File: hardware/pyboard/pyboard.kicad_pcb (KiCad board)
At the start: 2 copper layers, 65 parts, among them J1 Battery, J2 Arduino_Mega2560_Shield, J6 USB_B_Micro, J9 Micro_SD_SCHA5B0200, Q1 IRLML6402, Q2 IRLML6402, SW1 RST, SW2 USR, U1 STM32F405RGT6, U2 MCP1703A-3302_SOT89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

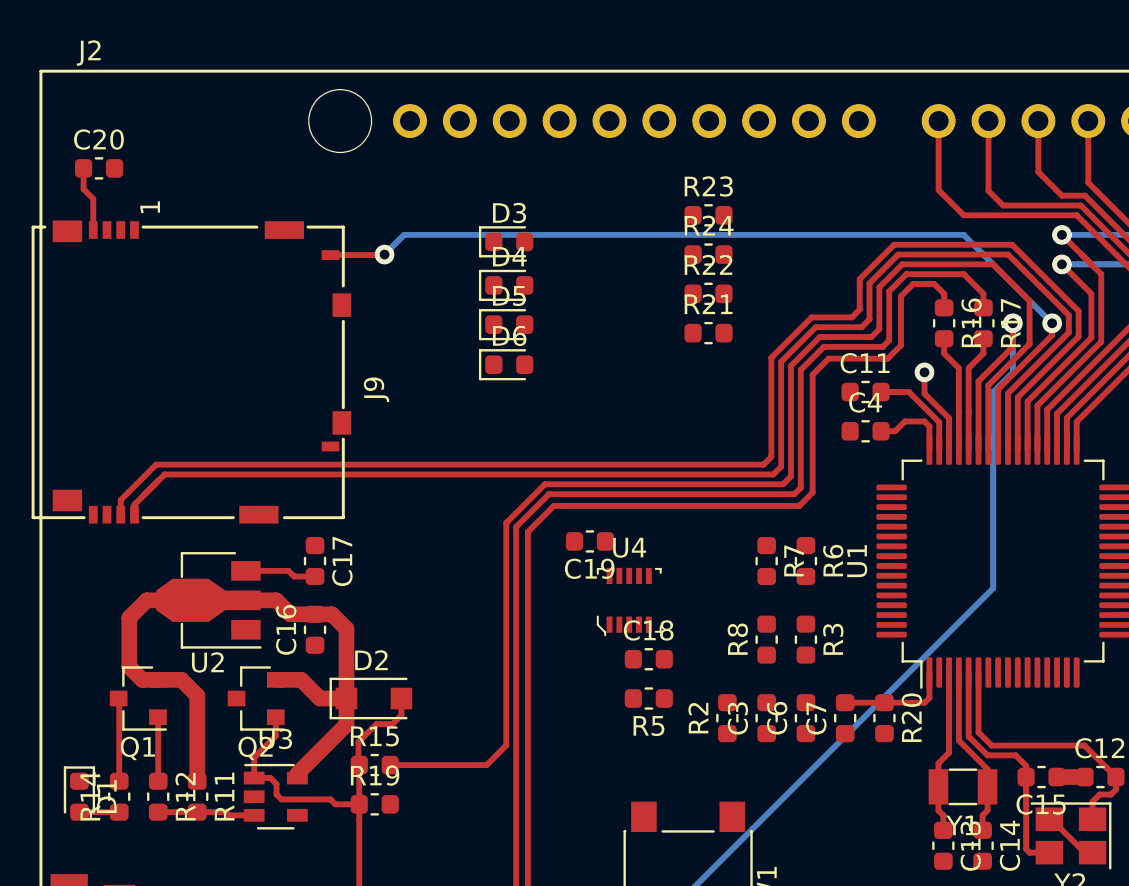
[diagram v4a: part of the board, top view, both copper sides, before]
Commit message: Add vias for SDIO and leds
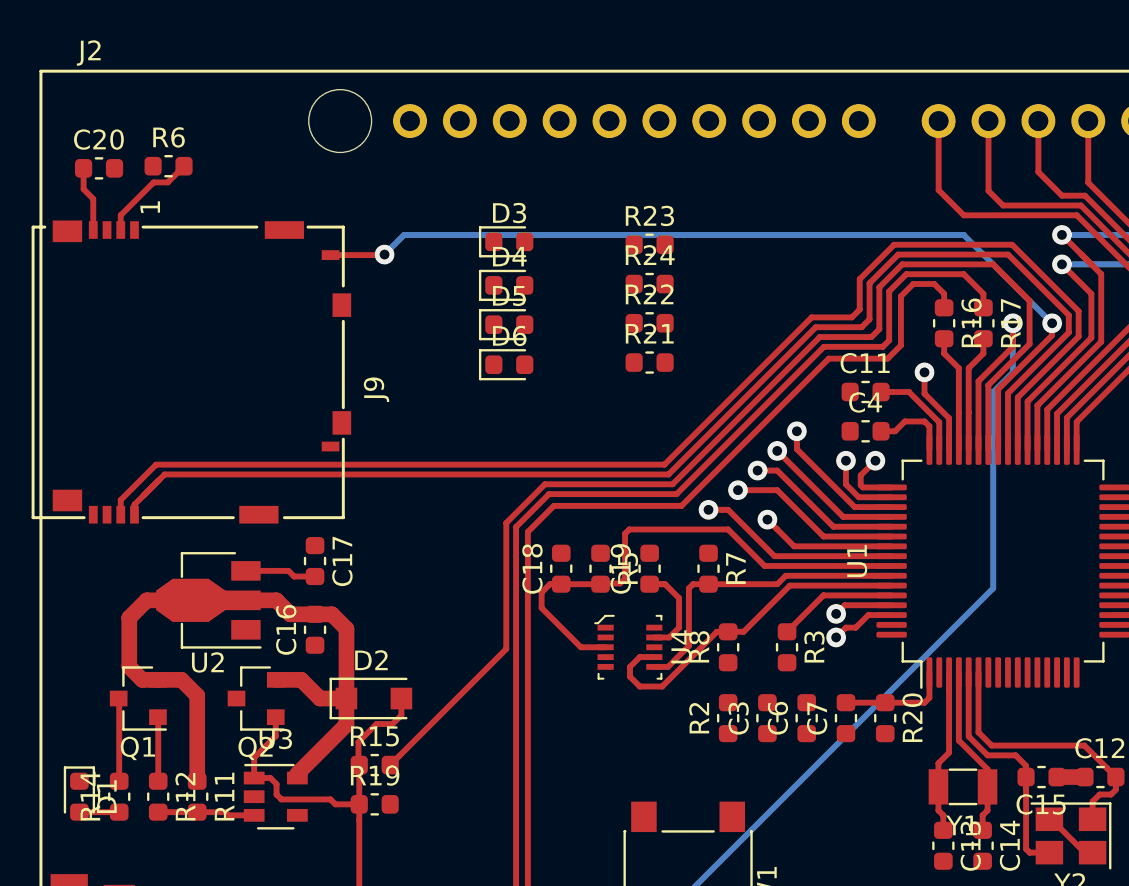
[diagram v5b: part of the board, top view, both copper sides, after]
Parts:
- moved R6 38.2 mm to (106.5, 71.5), turned to 0 degrees
- moved R5 7.05 mm to (128.5, 92.0), turned to 270 degrees
- moved C18 6.41 mm to (126.5, 92.0), turned to 90 degrees
- moved R21 3.35 mm to (131.0, 81.5)
- moved R22 3.35 mm to (131.0, 79.5)
- moved R23 3.35 mm to (131.0, 75.5)
- moved R24 3.35 mm to (131.0, 77.5)
- moved C19 3.34 mm to (131.0, 92.0), turned to 90 degrees
- moved R7 2.99 mm to (134.0, 92.0)
- moved U4 2.39 mm to (130.0, 96.0), turned to 270 degrees
- moved R8 2.00 mm to (135.0, 96.0)
- moved R3 1.04 mm to (138.0, 96.0)
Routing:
- net /MMA_AVDD: track 0.00 -> 26.1 mm
- net /SDA: track 0.00 -> 17.6 mm
- net /SCL: track 0.00 -> 15.7 mm
- net /SDIO_D3: track 0.00 -> 12.2 mm, vias 0 -> 1
- net /BLU: track 0.00 -> 10.3 mm, vias 0 -> 1
- net /SDIO_CMD: track 0.00 -> 8.80 mm, vias 0 -> 1
- net /SDIO_CK: track 0.00 -> 8.01 mm, vias 0 -> 1
- net /SDIO_D2: track 0.00 -> 6.96 mm, vias 0 -> 1
- net /SW: track 0.00 -> 6.89 mm, vias 0 -> 1
- net /VBUS: track 63.5 -> 57.4 mm
- net /BOOT0: track 0.00 -> 6.09 mm
- net +3V3: track 16.4 -> 21.9 mm
- net /YEL: track 0.00 -> 3.80 mm, vias 0 -> 1
- net /USB_D+: track 73.3 -> 69.8 mm
- net /USB_D-: track 75.6 -> 72.1 mm
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
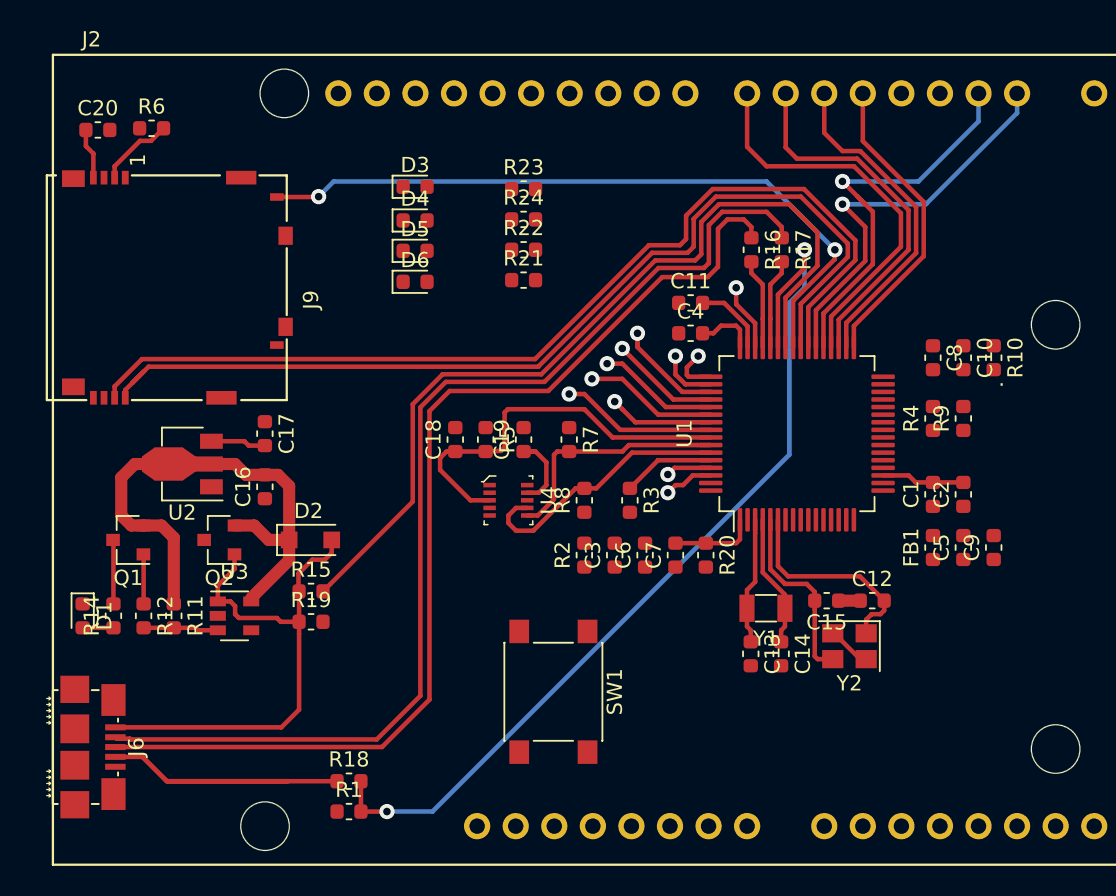
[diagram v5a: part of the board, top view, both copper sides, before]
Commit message: Retrace USB and sd card
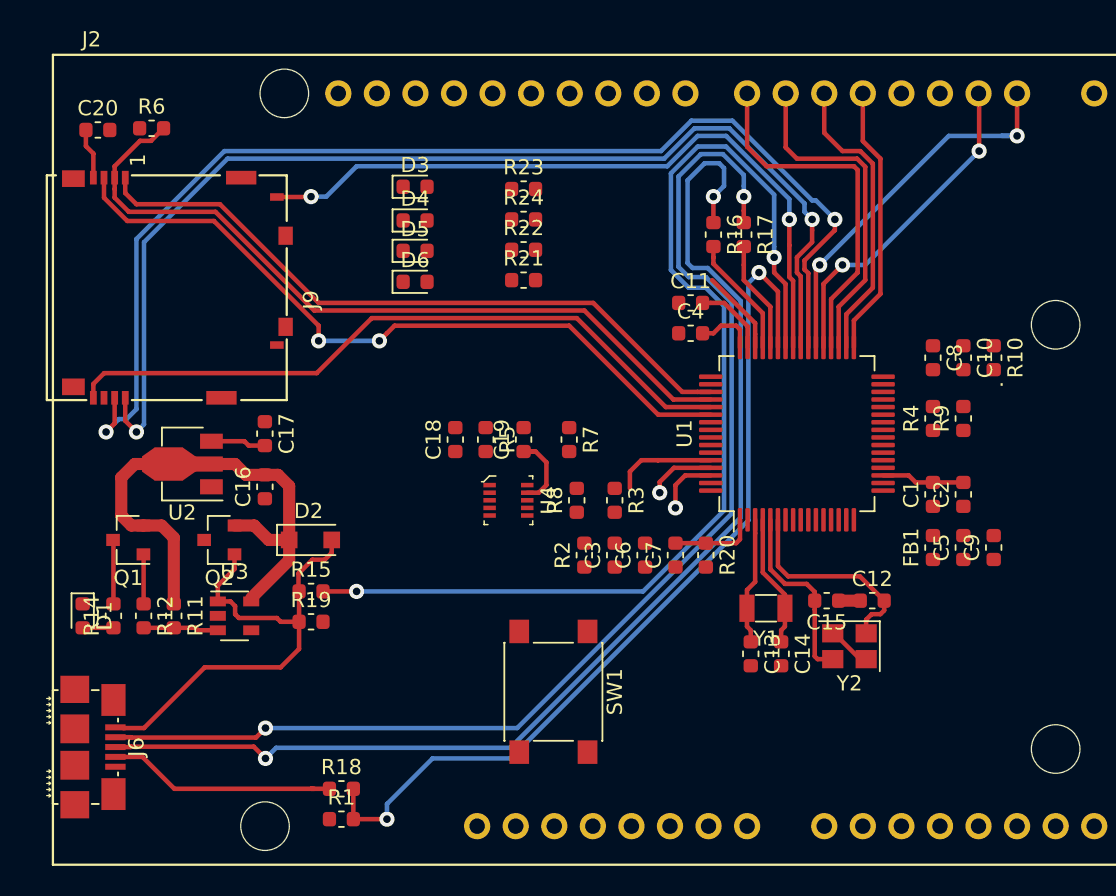
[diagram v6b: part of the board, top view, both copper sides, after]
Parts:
- moved R16 2.69 mm to (143.5, 78.5)
- moved R17 2.69 mm to (145.5, 78.5)
- moved R3 1.00 mm to (137.0, 96.0)
- moved R1 0.71 mm to (119.0, 117.0)
- moved R18 0.71 mm to (119.0, 115.0)
- moved R8 0.50 mm to (134.5, 96.0)
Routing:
- net /SDIO_CMD: track 8.80 -> 48.6 mm, vias 1 -> 2
- net /SDIO_D3: track 12.2 -> 51.1 mm, vias 1 -> 0
- net /SDIO_D2: track 6.96 -> 45.0 mm, vias 1 -> 0
- net /SDIO_CK: track 8.01 -> 45.8 mm, vias 1 -> 0
- net /MMA_AVDD: track 26.1 -> 0.00 mm
- net /SDA: track 17.6 -> 0.00 mm
- net /SCL: track 15.7 -> 0.00 mm
- net /VBUS: track 57.4 -> 72.2 mm, vias 0 -> 2
- net /SDIO_D0: track 65.6 -> 77.6 mm, vias 0 -> 2
- net /USB_ID: track 25.5 -> 15.2 mm
- net /BLU: track 10.3 -> 0.00 mm, vias 1 -> 0
- net /USB_D+: track 69.8 -> 79.2 mm, vias 0 -> 2
- net /SDIO_D1: track 64.9 -> 74.1 mm, vias 0 -> 2
- net /USB_D-: track 72.1 -> 79.9 mm, vias 0 -> 2
- net /SW: track 6.89 -> 0.00 mm, vias 1 -> 0
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
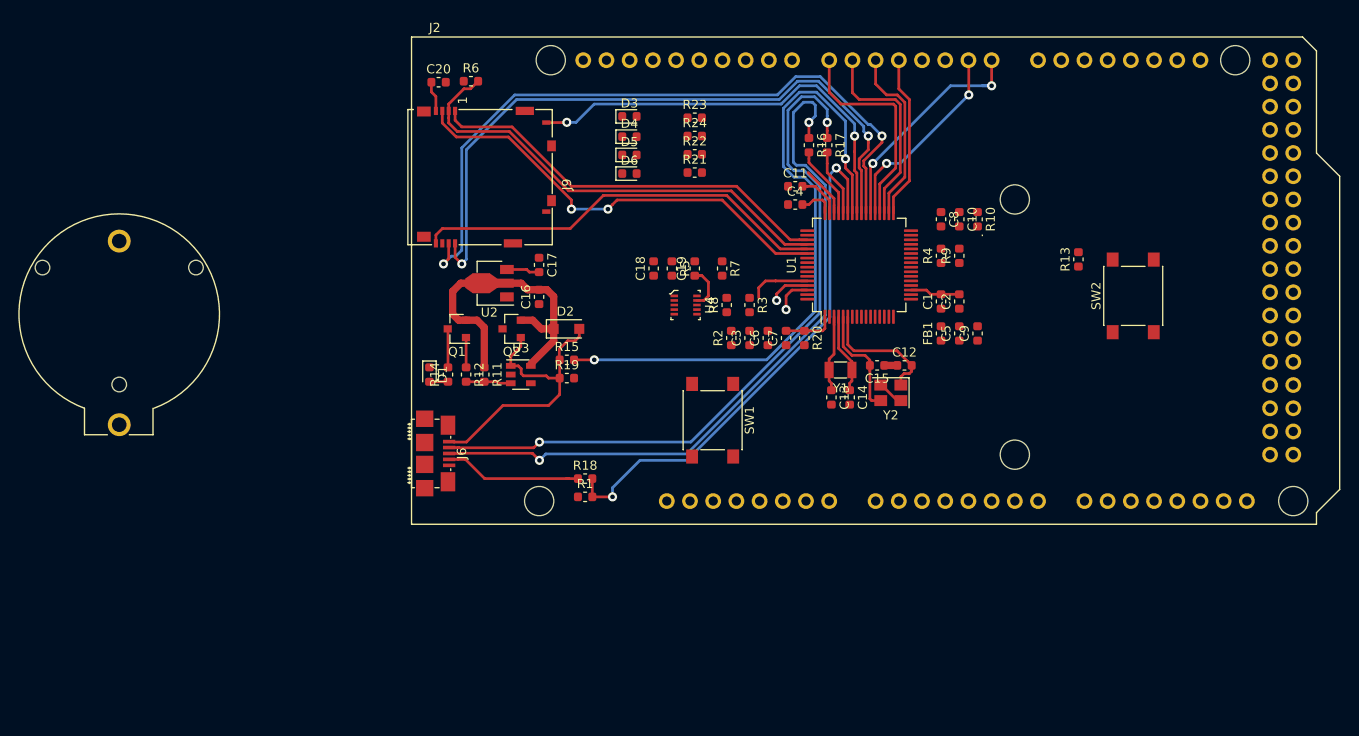
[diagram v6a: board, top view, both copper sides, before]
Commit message: Trace left part of the board
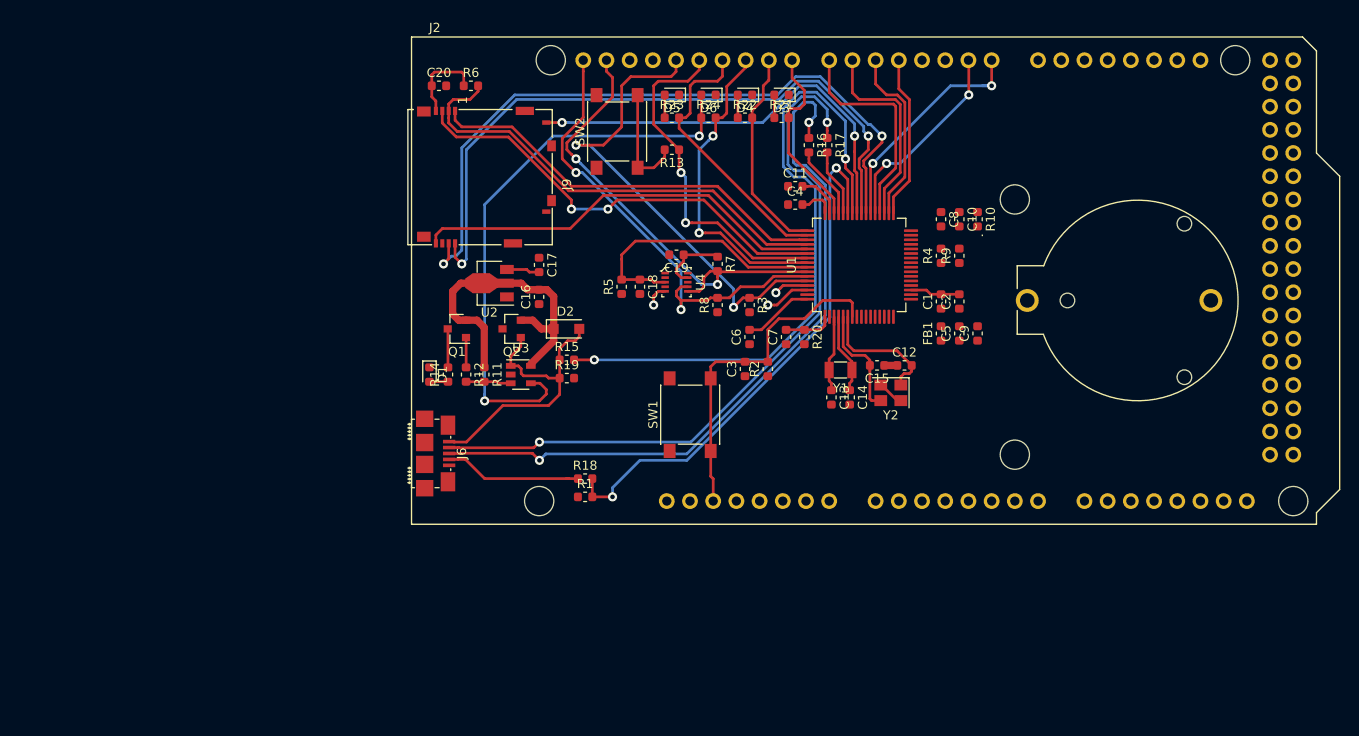
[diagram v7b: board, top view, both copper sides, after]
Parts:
- moved J1 111.5 mm to (179.5, 95.5), turned to 270 degrees
- moved SW2 59.3 mm to (122.5, 77.0)
- moved R13 46.1 mm to (128.5, 79.0), turned to 180 degrees
- moved D3 16.8 mm to (140.5, 73.0), turned to 180 degrees
- moved D4 13.4 mm to (136.5, 73.0), turned to 180 degrees
- moved D6 12.2 mm to (132.5, 73.0), turned to 180 degrees
- moved R21 11.2 mm to (140.5, 75.5)
- moved D5 8.05 mm to (128.5, 73.0), turned to 180 degrees
- moved R22 6.80 mm to (136.5, 75.5)
- moved R5 5.85 mm to (123.0, 94.0), turned to 90 degrees
- moved R2 5.24 mm to (139.0, 103.0)
- moved C3 3.43 mm to (136.5, 103.0)
- moved U4 2.69 mm to (129.0, 93.5)
- moved SW1 2.53 mm to (130.5, 108.0), turned to 90 degrees
- moved C18 2.50 mm to (125.0, 94.0), turned to 270 degrees
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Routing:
- net /B: track 0.00 -> 62.7 mm, vias 0 -> 2
- net /SDA: track 0.00 -> 52.6 mm, vias 0 -> 2
- net /SCL: track 0.00 -> 50.8 mm, vias 0 -> 2
- net /BOOT0: track 6.74 -> 53.2 mm, vias 0 -> 2
- net /SW: track 0.00 -> 38.1 mm, vias 0 -> 2
- net /~RST: track 0.00 -> 37.0 mm
- net /BLU: track 0.00 -> 35.4 mm, vias 0 -> 2
- net /YEL: track 0.00 -> 30.2 mm
- net /MMA_AVDD: track 0.00 -> 29.7 mm
- net /GRN: track 0.00 -> 23.4 mm
- net +3V3: track 21.9 -> 37.5 mm
- net /RED: track 5.61 -> 20.6 mm
- net /USR-SW: track 0.00 -> 12.2 mm
- net /Y: track 0.00 -> 2.50 mm
- net /R: track 0.00 -> 2.50 mm
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
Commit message: Trace bottom
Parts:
- moved R9 31.2 mm to (186.0, 73.5)
- moved R4 8.61 mm to (166.5, 89.5), turned to 180 degrees
- moved C5 3.04 mm to (163.0, 99.6)
- moved C9 3.04 mm to (165.0, 99.6)
- moved FB1 3.04 mm to (161.0, 99.6)
- moved J1 2.14 mm to (180.0, 93.4), turned to 0 degrees
- moved C10 2.06 mm to (159.5, 84.6)
- moved C8 2.06 mm to (157.5, 84.6)
- moved R10 2.06 mm to (161.5, 84.6)
- moved C1 2.00 mm to (160.0, 95.6)
- moved C2 2.00 mm to (162.0, 95.6)
- moved C12 1.49 mm to (154.5, 104.0)
- moved C15 1.39 mm to (151.0, 104.0)
- moved Y2 1.39 mm to (152.5, 107.0)
- moved C13 1.00 mm to (145.5, 107.0)
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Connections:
- J2 pad A0: /X1 -> /X19
- J2 pad A1: /X2 -> /X20
- J2 pad A10: /X21 -> (no net)
- J2 pad A11: /X22 -> (no net)
- J2 pad A12: /Y11 -> (no net)
- J2 pad A13: /Y12 -> (no net)
- J2 pad A2: /X5 -> /X21
- J2 pad A3: /X6 -> /X22
- J2 pad A4: /X7 -> /X1
- J2 pad A5: /X8 -> /X2
- J2 pad A6: /X11 -> /X3
- J2 pad A7: /X12 -> /X4
- J2 pad A8: /X19 -> (no net)
- J2 pad A9: /X20 -> (no net)
- J2 pad D14: /X3 -> (no net)
- J2 pad D15: /X4 -> (no net)
- J2 pad D22: (no net) -> /Y12
- J2 pad D24: (no net) -> /Y11
- J2 pad D26: (no net) -> /X12
- J2 pad D28: (no net) -> /X11
- J2 pad D30: (no net) -> /X8
- J2 pad D32: (no net) -> /X7
- J2 pad D34: (no net) -> /X6
- J2 pad D36: (no net) -> /X5
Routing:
- net /Y12: track 0.00 -> 52.1 mm
- net /Y11: track 0.00 -> 49.7 mm
- net /X12: track 0.00 -> 49.0 mm
- net /X8: track 0.00 -> 46.8 mm
- net /X11: track 0.00 -> 45.9 mm
- net /X7: track 0.00 -> 44.6 mm
- net /X6: track 0.00 -> 42.7 mm
- net /X5: track 0.00 -> 41.1 mm
- net /Y3: track 3.77 -> 38.3 mm, vias 1 -> 3
- net /X4: track 0.00 -> 32.9 mm
- net /Y4: track 5.00 -> 37.5 mm
- net /X18: track 0.00 -> 29.0 mm, vias 0 -> 2
- net /X19: track 0.00 -> 28.9 mm
- net /X20: track 0.00 -> 28.1 mm
- net /X3: track 0.00 -> 28.0 mm
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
